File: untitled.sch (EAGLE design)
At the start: 21 parts, among them IC1 ACS758LCB-050B-PFF-T

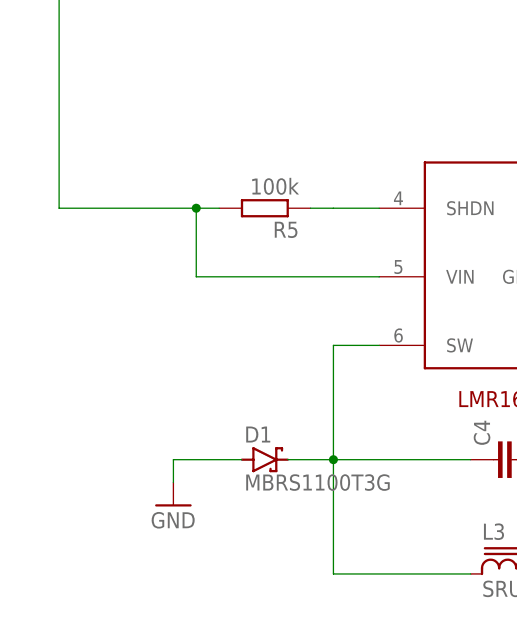
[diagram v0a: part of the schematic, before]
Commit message: Add TVS to power module
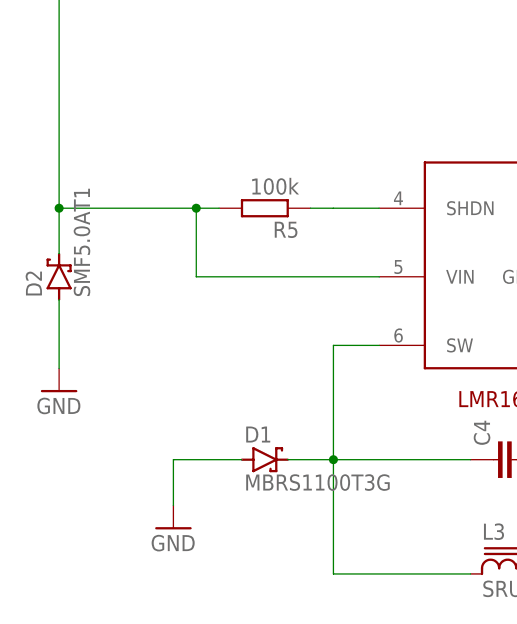
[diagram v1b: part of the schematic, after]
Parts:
- added D2: SMF5.0AT1, diode:SMF5.0AT1
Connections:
- net GND: now also D2.A
- net N$4: now also D2.C
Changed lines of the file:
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@@
 <grid distance="0.1" unitdist="inch" unit="inch" style="lines" multiple="1" display="no" altdistance="0.01" altunitdist="inch" altunit="inch"/>
 <layers>
-<layer number="1" name="Top" color="4" fill="1" visible="yes" active="no"/>
-<layer number="16" name="Bottom" color="1" fill="1" visible="yes" active="no"/>
-<layer number="17" name="Pads" color="2" fill="1" visible="yes" active="no"/>
-<layer number="18" name="Vias" color="2" fill="1" visible="yes" active="no"/>
-<layer number="19" name="Unrouted" color="6" fill="1" visible="yes" active="no"/>
-<layer number="20" name="Dimension" color="24" fill="1" visible="yes" active="no"/>
-<layer number="21" name="tPlace" color="7" fill="1" visible="yes" active="no"/>
-<layer number="22" name="bPlace" color="7" fill="1" visible="yes" active="no"/>
-<layer number="23" name="tOrigins" color="15" fill="1" visible="yes" active="no"/>
-<layer number="24" name="bOrigins" color="15" fill="1" visible="yes" active="no"/>
-<layer number="25" name="tNames" color="7" fill="1" visible="yes" active="no"/>
-<layer number="26" name="bNames" color="7" fill="1" visible="yes" active="no"/>
-<layer number="27" name="tValues" color="7" fill="1" visible="yes" active="no"/>
-<layer number="28" name="bValues" color="7" fill="1" visible="yes" active="no"/>
+<layer number="1" name="Top" color="4" fill="1" visible="no" active="no"/>
+<layer number="16" name="Bottom" color="1" fill="1" visible="no" active="no"/>
+<layer number="17" name="Pads" color="2" fill="1" visible="no" active="no"/>
+<layer number="18" name="Vias" color="2" fill="1" visible="no" active="no"/>
+<layer number="19" name="Unrouted" color="6" fill="1" visible="no" active="no"/>
+<layer number="20" name="Dimension" color="24" fill="1" visible="no" active="no"/>
+<layer number="21" name="tPlace" color="7" fill="1" visible="no" active="no"/>
+<layer number="22" name="bPlace" color="7" fill="1" visible="no" active="no"/>
+<layer number="23" name="tOrigins" color="15" fill="1" visible="no" active="no"/>
+<layer number="24" name="bOrigins" color="15" fill="1" visible="no" active="no"/>
+<layer number="25" name="tNames" color="7" fill="1" visible="no" active="no"/>
+<layer number="26" name="bNames" color="7" fill="1" visible="no" active="no"/>
+<layer number="27" name="tValues" color="7" fill="1" visible="no" active="no"/>
+<layer number="28" name="bValues" color="7" fill="1" visible="no" active="no"/>
 <layer number="29" name="tStop" color="7" fill="3" visible="no" active="no"/>
 <layer number="30" name="bStop" color="7" fill="6" visible="no" active="no"/>
@@
 <layer number="35" name="tGlue" color="7" fill="4" visible="no" active="no"/>
 <layer number="36" name="bGlue" color="7" fill="5" visible="no" active="no"/>
-<layer number="37" name="tTest" color="7" fill="1" visible="yes" active="no"/>
-<layer number="38" name="bTest" color="7" fill="1" visible="yes" active="no"/>
+<layer number="37" name="tTest" color="7" fill="1" visible="no" active="no"/>
+<layer number="38" name="bTest" color="7" fill="1" visible="no" active="no"/>
 <layer number="39" name="tKeepout" color="4" fill="11" visible="no" active="no"/>
 <layer number="40" name="bKeepout" color="1" fill="11" visible="no" active="no"/>
@@
 <layer number="44" name="Drills" color="7" fill="1" visible="no" active="no"/>
 <layer number="45" name="Holes" color="7" fill="1" visible="no" active="no"/>
-<layer number="46" name="Milling" color="3" fill="1" visible="yes" active="no"/>
-<layer number="47" name="Measures" color="7" fill="1" visible="yes" active="no"/>
-<layer number="48" name="Document" color="7" fill="1" visible="yes" active="no"/>
-<layer number="49" name="Reference" color="7" fill="1" visible="yes" active="no"/>
-<layer number="50" name="dxf" color="7" fill="1" visible="yes" active="no"/>
-<layer number="51" name="tDocu" color="7" fill="1" visible="yes" active="no"/>
-<layer number="52" name="bDocu" color="7" fill="1" visible="yes" active="no"/>
-<layer number="53" name="tGND_GNDA" color="7" fill="9" visible="yes" active="no"/>
-<layer number="54" name="bGND_GNDA" color="1" fill="9" visible="yes" active="no"/>
-<layer number="56" name="wert" color="7" fill="1" visible="yes" active="no"/>
-<layer number="57" name="tCAD" color="7" fill="1" visible="yes" active="no"/>
+<layer number="46" name="Milling" color="3" fill="1" visible="no" active="no"/>
+<layer number="47" name="Measures" color="7" fill="1" visible="no" active="no"/>
+<layer number="48" name="Document" color="7" fill="1" visible="no" active="no"/>
+<layer number="49" name="Reference" color="7" fill="1" visible="no" active="no"/>
+<layer number="50" name="dxf" color="7" fill="1" visible="no" active="no"/>
+<layer number="51" name="tDocu" color="7" fill="1" visible="no" active="no"/>
+<layer number="52" name="bDocu" color="7" fill="1" visible="no" active="no"/>
+<layer number="53" name="tGND_GNDA" color="7" fill="9" visible="no" active="no"/>
+<layer number="54" name="bGND_GNDA" color="1" fill="9" visible="no" active="no"/>
+<layer number="56" name="wert" color="7" fill="1" visible="no" active="no"/>
+<layer number="57" name="tCAD" color="7" fill="1" visible="no" active="no"/>
 <layer number="88" name="SimResults" color="9" fill="1" visible="yes" active="yes"/>
 <layer number="89" name="SimProbes" color="9" fill="1" visible="yes" active="yes"/>
@@
 <part name="C6" library="rcl" library_urn="urn:adsk.eagle:library:334" deviceset="CPOL-EU" device="R/2012-12R" package3d_urn="urn:adsk.eagle:package:23426/2" value="22uF 25V"/>
 <part name="L3" library="inductor-bourns" deviceset="SRU1038" device=""/>
+<part name="D2" library="diode" library_urn="urn:adsk.eagle:library:210" deviceset="SMF5.0AT1" device="" package3d_urn="urn:adsk.eagle:package:43458/1"/>
+<part name="GND11" library="supply1" library_urn="urn:adsk.eagle:library:371" deviceset="GND" device=""/>
 </parts>
 <sheets>
@@
 <attribute name="VALUE" x="10.414" y="-41.529" size="1.778" layer="96"/>
 </instance>
-<instance part="GND10" gate="1" x="2.54" y="-43.18" smashed="yes">
-<attribute name="VALUE" x="0" y="-45.72" size="1.778" layer="96"/>
+<instance part="GND10" gate="1" x="2.54" y="-45.72" smashed="yes">
+<attribute name="VALUE" x="0" y="-48.26" size="1.778" layer="96"/>
 </instance>
 <instance part="C2" gate="G$1" x="7.62" y="35.56" smashed="yes">
@@
 <attribute name="NAME" x="36.83" y="-46.99" size="1.778" layer="95"/>
 <attribute name="VALUE" x="36.83" y="-53.34" size="1.778" layer="96"/>
+</instance>
+<instance part="D2" gate="G$1" x="-10.16" y="-17.78" smashed="yes" rot="R90">
+<attribute name="NAME" x="-12.065" y="-20.066" size="1.778" layer="95" rot="R90"/>
+<attribute name="VALUE" x="-6.731" y="-20.066" size="1.778" layer="96" rot="R90"/>
+</instance>
+<instance part="GND11" gate="1" x="-10.16" y="-30.48" smashed="yes">
+<attribute name="VALUE" x="-12.7" y="-33.02" size="1.778" layer="96"/>
 </instance>
 </instances>
@@
 <wire x1="10.16" y1="-38.1" x2="2.54" y2="-38.1" width="0.1524" layer="91"/>
 <pinref part="GND10" gate="1" pin="GND"/>
-<wire x1="2.54" y1="-38.1" x2="2.54" y2="-40.64" width="0.1524" layer="91"/>
+<wire x1="2.54" y1="-38.1" x2="2.54" y2="-43.18" width="0.1524" layer="91"/>
 </segment>
 <segment>
@@
 <pinref part="GND8" gate="1" pin="GND"/>
 <pinref part="C6" gate="G$1" pin="-"/>
+</segment>
+<segment>
+<pinref part="D2" gate="G$1" pin="A"/>
+<wire x1="-10.16" y1="-20.32" x2="-10.16" y2="-27.94" width="0.1524" layer="91"/>
+<pinref part="GND11" gate="1" pin="GND"/>
 </segment>
 </net>
@@
 <pinref part="C2" gate="G$1" pin="+"/>
 <junction x="7.62" y="38.1"/>
+<pinref part="D2" gate="G$1" pin="C"/>
+<wire x1="-10.16" y1="-10.16" x2="-10.16" y2="-15.24" width="0.1524" layer="91"/>
+<junction x="-10.16" y="-10.16"/>
 </segment>
 </net>

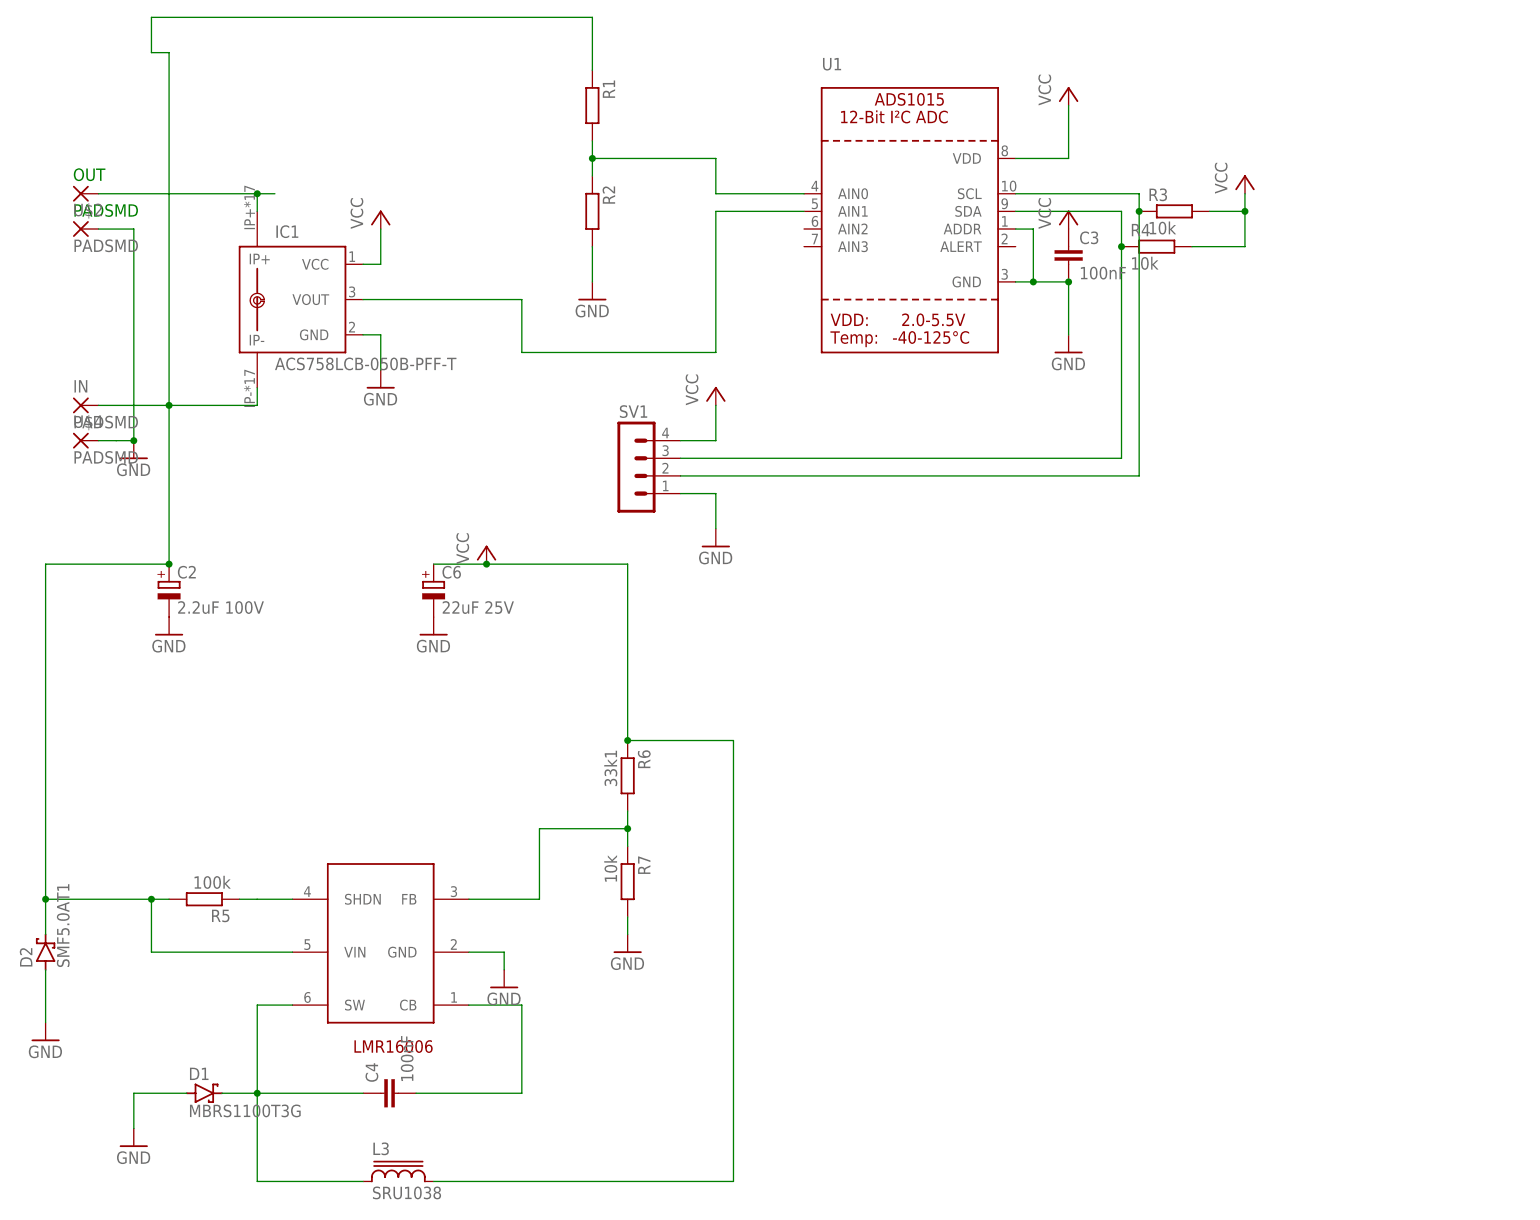
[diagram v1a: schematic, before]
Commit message: Update scheamictic to include dedicated ldo for senors and p mosfeto control power for sensors
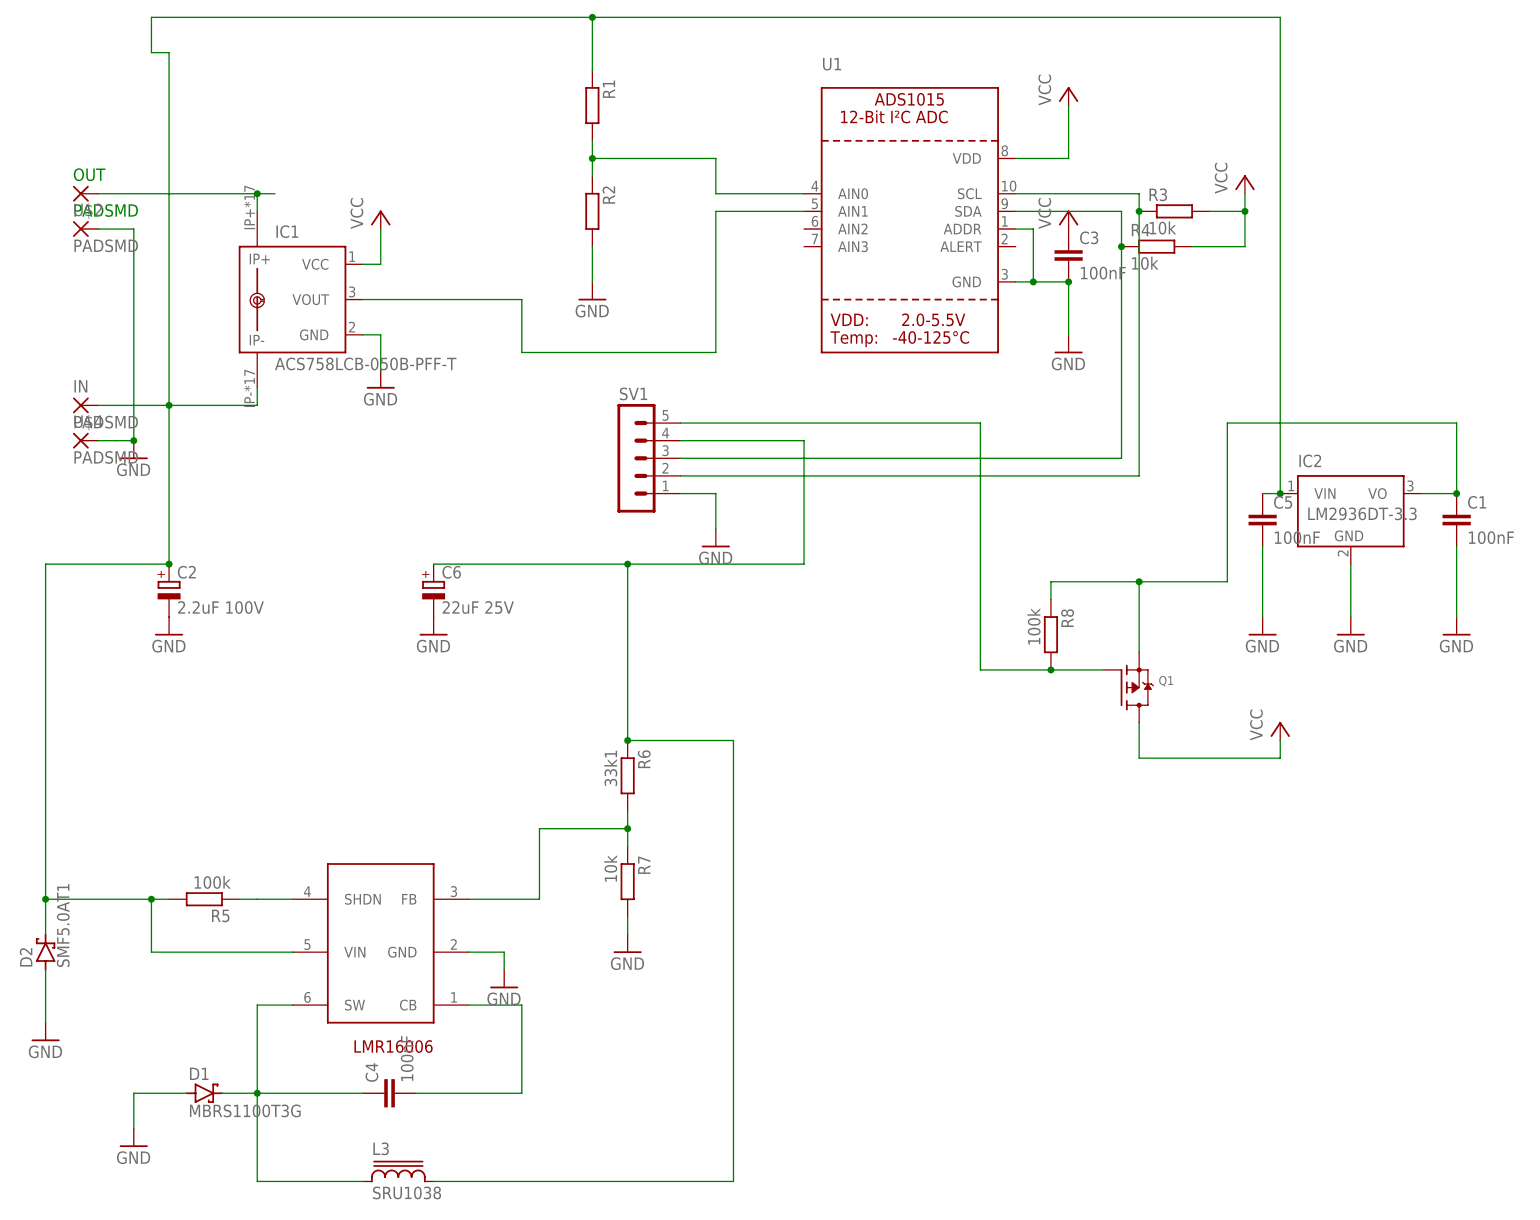
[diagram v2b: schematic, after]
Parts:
- added C1, C5: 100nF, rcl:C-EUC0805
- added IC2: LM2936DT-3.3, national-semiconductor:LM2936DT-3.3
- added Q1: (no value), microbuilder:MOSFET-PWIDE
- added R8: 100k, rcl:R-EU_R0805
- SV1: device con-lstb:MA04-1 -> con-lstb:MA05-1
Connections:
- new net N$12: C1.1, IC2.VO, Q1.S, R8.1
- new net N$7: Q1.G, R8.2, SV1.5
- new net N$8: C6.+, L3.2, R6.1, SV1.4
- net GND: now also C1.2, C5.2, IC2.GND
- net N$4: now also C5.1, IC2.VIN
- net VCC: now also Q1.D; no longer C6.+, L3.2, R6.1, SV1.4
